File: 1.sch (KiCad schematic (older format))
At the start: 46 parts, among them J1 USB_B_Micro, J10 SPI2, J11 Micro_SD_Card, J2 Power, J3 SWD, J4 Protected, J5 ADC, J6 SPI1, J7 UART1, J8 BxI2C1, J9 I2C2, K1 NRST, K2 WKUP, K3 KPA0, U1 STM32F103C8Tx, U2 AMS1117-3.3, Y1 8MHz, Y2 32.768k

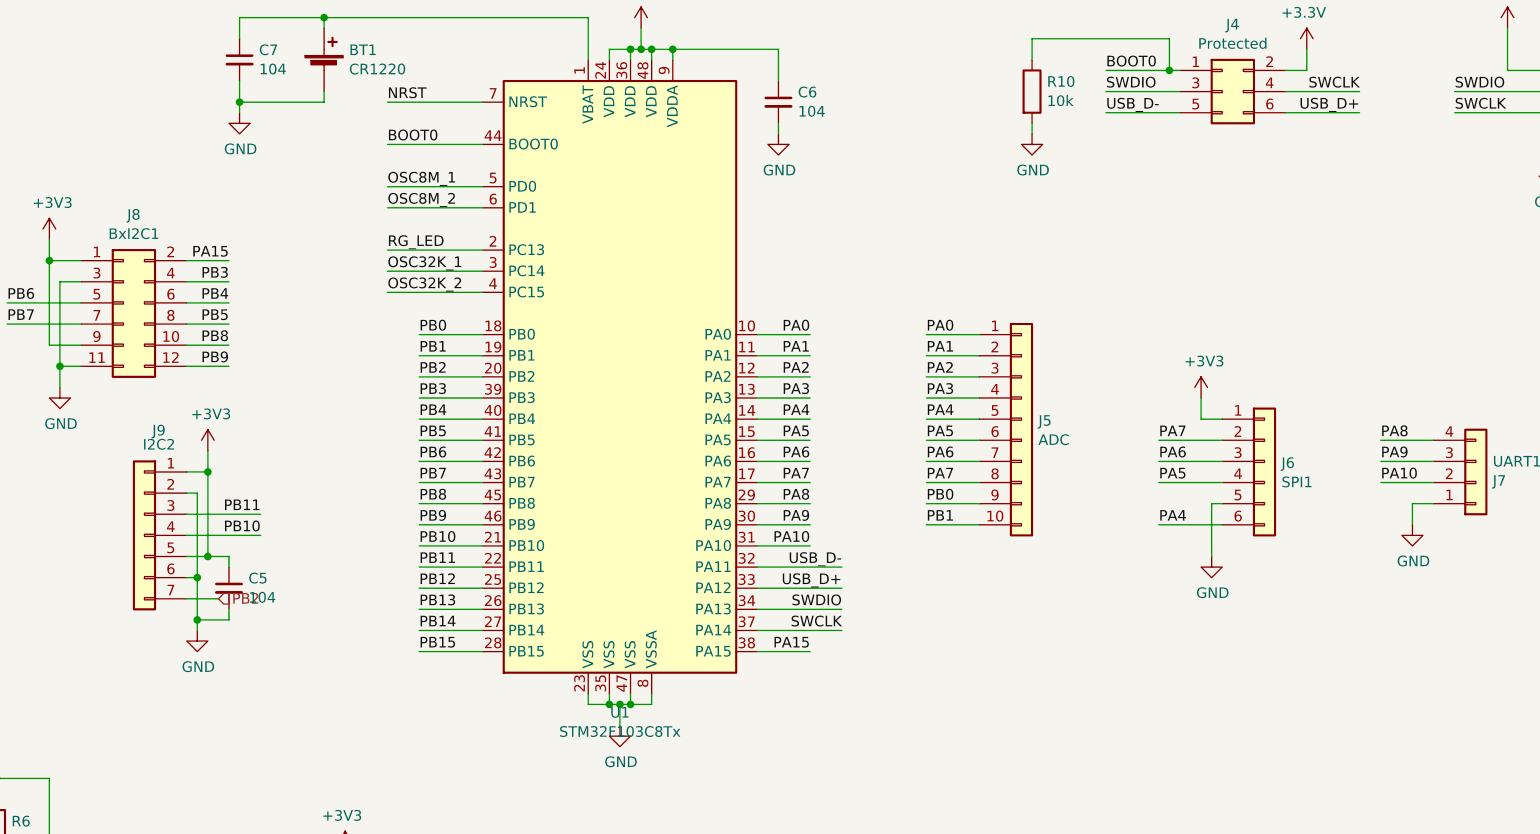
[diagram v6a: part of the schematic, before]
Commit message: add PinSocket
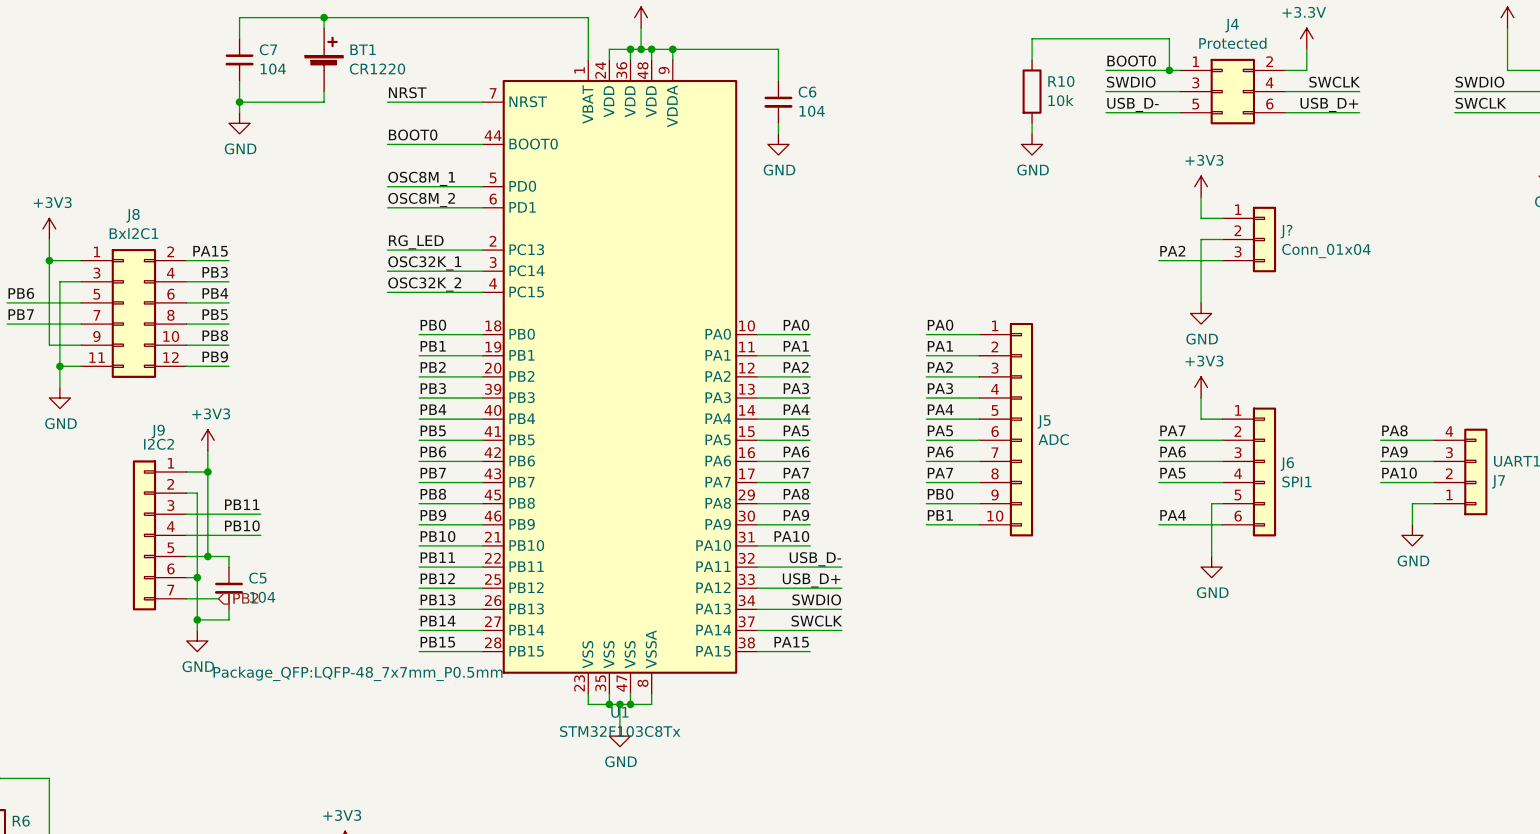
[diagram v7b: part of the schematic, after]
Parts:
- added J?: Conn_01x04, Connector_PinSocket_2.54mm:PinSocket_1x03_P2.54mm_Vertical, symbol Connector_Generic:Conn_01x03
- J10: footprint Connector_PinHeader_2.54mm:PinHeader_1x06_P2.54mm_Vertical -> Connector_PinSocket_2.54mm:PinSocket_1x06_P2.54mm_Vertical
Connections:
- net +3V3: now also J?.1 (Pin_1)
- net GND: now also J?.2 (Pin_2)
- net PA2: now also J?.3 (Pin_3)
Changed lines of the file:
@@
 F 0 "U1" H 6200 2561 50  0000 C CNN
 F 1 "STM32F103C8Tx" H 6200 2470 50  0000 C CNN
-F 2 "Package_QFP:LQFP-48_7x7mm_P0.5mm" H 5650 2750 50  0001 R CNN
+F 2 "Package_QFP:LQFP-48_7x7mm_P0.5mm" H 5650 2750 50  0000 R CNN
 F 3 "http://www.st.com/st-web-ui/static/active/en/resource/technical/document/datasheet/CD00161566.pdf" H 6250 4150 50  0001 C CNN
 	1    6250 4150
@@
 F 0 "J10" H 4680 6692 50  0000 L CNN
 F 1 "SPI2" H 4680 6601 50  0000 L CNN
-F 2 "Connector_PinHeader_2.54mm:PinHeader_1x06_P2.54mm_Vertical" H 4680 6555 50  0001 L CNN
+F 2 "Connector_PinSocket_2.54mm:PinSocket_1x06_P2.54mm_Vertical" H 4680 6555 50  0001 L CNN
 F 3 "~" H 4600 6700 50  0001 C CNN
 	1    4600 6700
@@
 	1    0    0    -1
 $EndComp
+$Comp
+L Connector_Generic:Conn_01x03 J?
+U 1 1 609759C3
+P 9250 3500
+F 0 "J?" H 9330 3542 50  0000 L CNN
+F 1 "Conn_01x04" H 9330 3451 50  0000 L CNN
+F 2 "Connector_PinSocket_2.54mm:PinSocket_1x03_P2.54mm_Vertical" H 9250 3500 50  0001 C CNN
+F 3 "~" H 9250 3500 50  0001 C CNN
+	1    9250 3500
+	1    0    0    -1
+$EndComp
+Wire Wire Line
+	8950 3400 9050 3400
+$Comp
+L power:+3V3 #PWR?
+U 1 1 6097B24C
+P 8950 3300
+F 0 "#PWR?" H 8950 3150 50  0001 C CNN
+F 1 "+3V3" H 8965 3473 50  0000 C CNN
+F 2 "" H 8950 3300 50  0001 C CNN
+F 3 "" H 8950 3300 50  0001 C CNN
+	1    8950 3300
+	1    0    0    -1
+$EndComp
+Wire Wire Line
+	8950 3300 8950 3400
+Text Label 8750 3600 0    50   ~ 0
+PA2
+Wire Wire Line
+	9050 3500 8950 3500
+Wire Wire Line
+	8950 3500 8950 3800
+$Comp
+L power:GND #PWR?
+U 1 1 60995CA3
+P 8950 3800
+F 0 "#PWR?" H 8950 3550 50  0001 C CNN
+F 1 "GND" H 8955 3627 50  0000 C CNN
+F 2 "" H 8950 3800 50  0001 C CNN
+F 3 "" H 8950 3800 50  0001 C CNN
+	1    8950 3800
+	1    0    0    -1
+$EndComp
+Wire Wire Line
+	8750 3600 9050 3600
 $EndSCHEMATC

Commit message: save .sch file
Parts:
- gave numbers to parts that had none: 1
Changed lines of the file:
@@
 $EndComp
 $Comp
-L Connector_Generic:Conn_01x03 J?
+L Connector_Generic:Conn_01x03 J12
 U 1 1 609759C3
 P 9250 3500
-F 0 "J?" H 9330 3542 50  0000 L CNN
+F 0 "J12" H 9330 3542 50  0000 L CNN
 F 1 "Conn_01x04" H 9330 3451 50  0000 L CNN
 F 2 "Connector_PinSocket_2.54mm:PinSocket_1x03_P2.54mm_Vertical" H 9250 3500 50  0001 C CNN
@@
 	8950 3400 9050 3400
 $Comp
-L power:+3V3 #PWR?
+L power:+3V3 #PWR0134
 U 1 1 6097B24C
 P 8950 3300
-F 0 "#PWR?" H 8950 3150 50  0001 C CNN
+F 0 "#PWR0134" H 8950 3150 50  0001 C CNN
 F 1 "+3V3" H 8965 3473 50  0000 C CNN
 F 2 "" H 8950 3300 50  0001 C CNN
@@
 	8950 3500 8950 3800
 $Comp
-L power:GND #PWR?
+L power:GND #PWR0135
 U 1 1 60995CA3
 P 8950 3800
-F 0 "#PWR?" H 8950 3550 50  0001 C CNN
+F 0 "#PWR0135" H 8950 3550 50  0001 C CNN
 F 1 "GND" H 8955 3627 50  0000 C CNN
 F 2 "" H 8950 3800 50  0001 C CNN
